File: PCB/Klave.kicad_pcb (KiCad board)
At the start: 2 copper layers, 156.3 x 127.5 mm, 87 parts, among them J1 6P6C, J2 OLED, SW0 Reset, SW1 0:0, SW10 1:3, SW11 1:4, SW12 1:5, SW13 2:0, SW14 2:1, SW15 2:2, SW16 2:3, SW17 2:4, SW18 2:5, SW19 3:0, SW2 0:1, SW20 3:1, SW21 3:2, SW22 3:3, SW23 3:4, SW24 3:5, SW26 4:1, SW27 4:2, SW28 4:3, SW29 4:4, SW3 0:2, SW30 4:5, SW35 5:4, SW36 5:5, SW4 0:3, SW5 0:4, SW6 0:5, SW7 1:0, SW8 1:1, SW9 1:2, U1 ProMicro

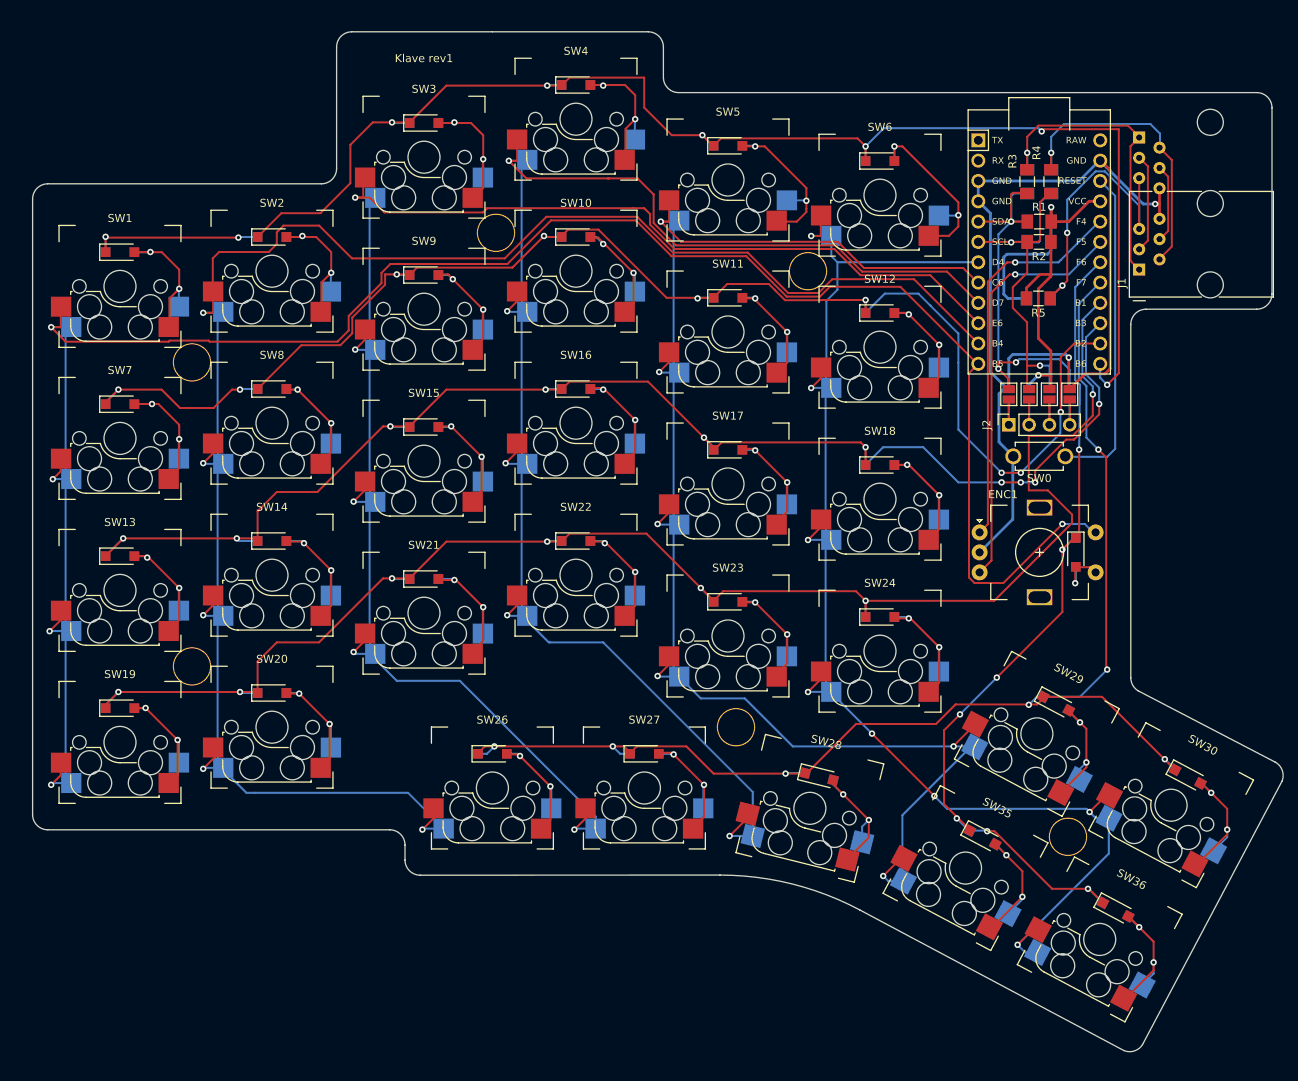
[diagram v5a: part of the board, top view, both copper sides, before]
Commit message: Add GND vias
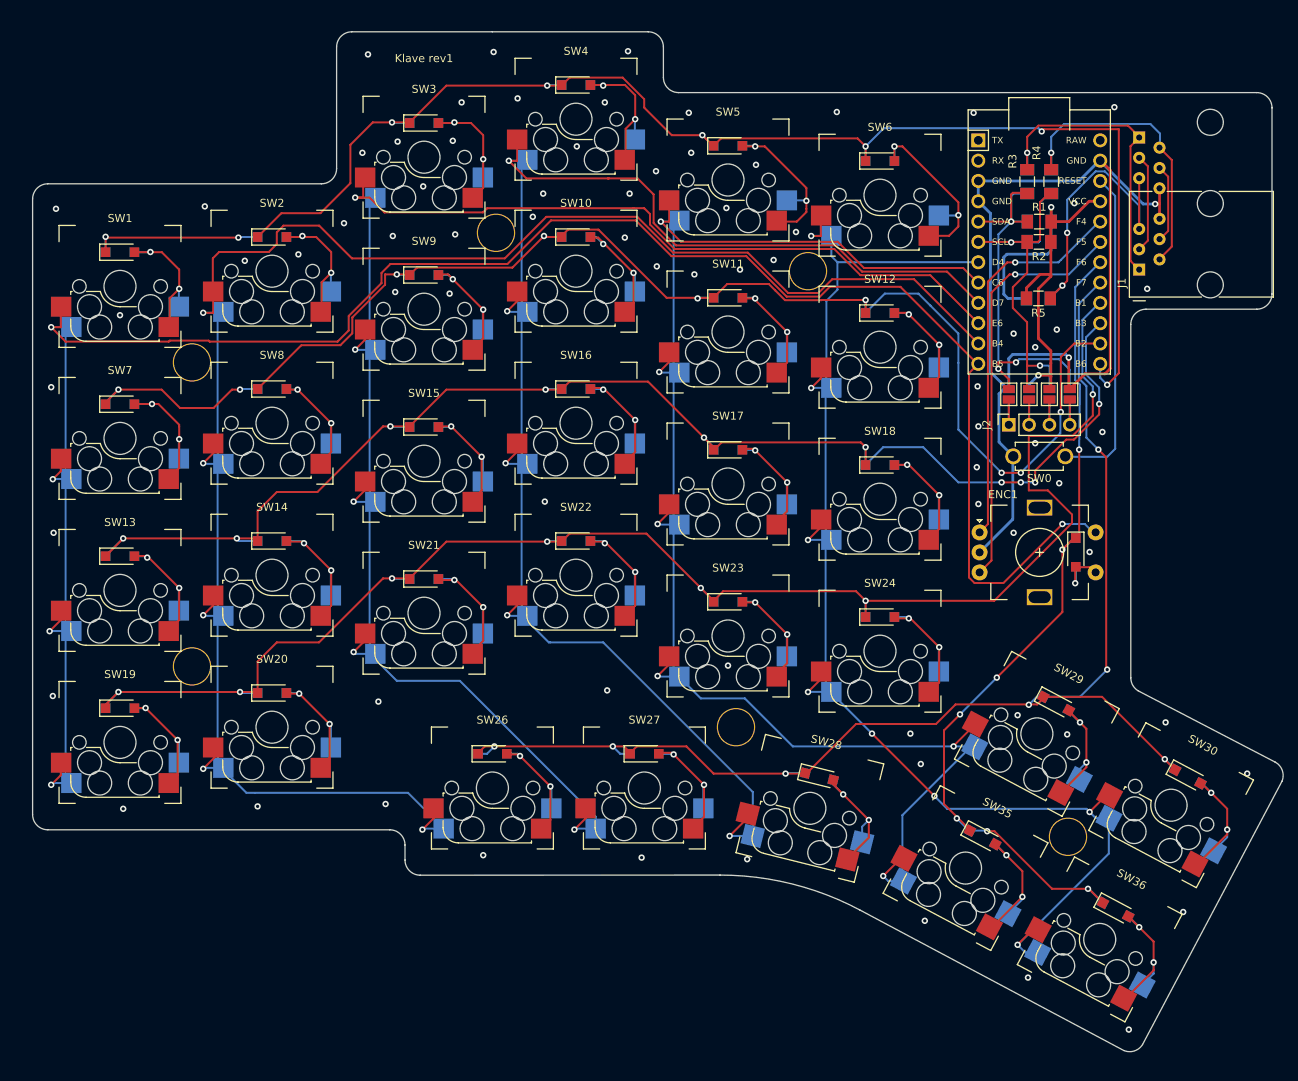
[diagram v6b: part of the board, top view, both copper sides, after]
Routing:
- net row0: track 194.5 -> 192.9 mm
- net GND: vias 2 -> 77
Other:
- rule trace_min: 0.2 -> 0.25
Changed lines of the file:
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@@
     (thickness 1.6)
     (drawings 36)
-    (tracks 1093)
+    (tracks 1169)
     (zones 0)
     (modules 87)
@@
     (zone_clearance 0.508)
     (zone_45_only no)
-    (trace_min 0.2)
+    (trace_min 0.25)
     (via_size 0.8)
     (via_drill 0.4)
@@
   (segment (start 158.626699 69.831301) (end 161.128625 69.831301) (width 0.35) (layer F.Cu) (net 34))
   (segment (start 161.779301 44.379301) (end 160.6 43.2) (width 0.35) (layer F.Cu) (net 34))
+  (via (at 160.8 77.1) (size 0.8) (drill 0.4) (layers F.Cu B.Cu) (net 34))
+  (via (at 157.3 48.5) (size 0.8) (drill 0.4) (layers F.Cu B.Cu) (net 34))
+  (via (at 114 106.3) (size 0.8) (drill 0.4) (layers F.Cu B.Cu) (net 34))
+  (via (at 136.8 114.8) (size 0.8) (drill 0.4) (layers F.Cu B.Cu) (net 34))
+  (via (at 138.1 118.6) (size 0.8) (drill 0.4) (layers F.Cu B.Cu) (net 34))
+  (via (at 149.7 89.7) (size 0.8) (drill 0.4) (layers F.Cu B.Cu) (net 34))
+  (via (at 155.4 83.5) (size 0.8) (drill 0.4) (layers F.Cu B.Cu) (net 34))
+  (via (at 145.3 86.1) (size 0.8) (drill 0.4) (layers F.Cu B.Cu) (net 34))
+  (via (at 145.1 81.5) (size 0.8) (drill 0.4) (layers F.Cu B.Cu) (net 34))
+  (via (at 145.3 76.4) (size 0.8) (drill 0.4) (layers F.Cu B.Cu) (net 34))
+  (via (at 145.2 71.4) (size 0.8) (drill 0.4) (layers F.Cu B.Cu) (net 34))
+  (via (at 149.7 64.8) (size 0.8) (drill 0.4) (layers F.Cu B.Cu) (net 34))
+  (via (at 152.4 66.5) (size 0.8) (drill 0.4) (layers F.Cu B.Cu) (net 34))
+  (via (at 155.1 64.3) (size 0.8) (drill 0.4) (layers F.Cu B.Cu) (net 34))
+  (via (at 119.7 55.6) (size 0.8) (drill 0.4) (layers F.Cu B.Cu) (net 34))
+  (via (at 115.5 56.8) (size 0.8) (drill 0.4) (layers F.Cu B.Cu) (net 34))
+  (via (at 109.8 57.4) (size 0.8) (drill 0.4) (layers F.Cu B.Cu) (net 34))
+  (via (at 105.1 56.4) (size 0.8) (drill 0.4) (layers F.Cu B.Cu) (net 34))
+  (via (at 101.1 52.8) (size 0.8) (drill 0.4) (layers F.Cu B.Cu) (net 34))
+  (via (at 90.9 47.3) (size 0.8) (drill 0.4) (layers F.Cu B.Cu) (net 34))
+  (via (at 101.7 47.3) (size 0.8) (drill 0.4) (layers F.Cu B.Cu) (net 34))
+  (via (at 105 44.5) (size 0.8) (drill 0.4) (layers F.Cu B.Cu) (net 34))
+  (via (at 109.4 42.2) (size 0.8) (drill 0.4) (layers F.Cu B.Cu) (net 34))
+  (via (at 117.5 43.7) (size 0.8) (drill 0.4) (layers F.Cu B.Cu) (net 34))
+  (via (at 98.6 35.9) (size 0.8) (drill 0.4) (layers F.Cu B.Cu) (net 34))
+  (via (at 80.7 35.9) (size 0.8) (drill 0.4) (layers F.Cu B.Cu) (net 34))
+  (via (at 87.7 35.4) (size 0.8) (drill 0.4) (layers F.Cu B.Cu) (net 34))
+  (via (at 79.9 52.4) (size 0.8) (drill 0.4) (layers F.Cu B.Cu) (net 34))
+  (via (at 72.1 52.6) (size 0.8) (drill 0.4) (layers F.Cu B.Cu) (net 34))
+  (via (at 66 51) (size 0.8) (drill 0.4) (layers F.Cu B.Cu) (net 34))
+  (via (at 60.3 54.9) (size 0.8) (drill 0.4) (layers F.Cu B.Cu) (net 34))
+  (via (at 79.6 40.7) (size 0.8) (drill 0.4) (layers F.Cu B.Cu) (net 34))
+  (via (at 72.7 40.8) (size 0.8) (drill 0.4) (layers F.Cu B.Cu) (net 34))
+  (via (at 68.3 42.2) (size 0.8) (drill 0.4) (layers F.Cu B.Cu) (net 34))
+  (via (at 38 62.5) (size 0.8) (drill 0.4) (layers F.Cu B.Cu) (net 34))
+  (via (at 53.6 55.7) (size 0.8) (drill 0.4) (layers F.Cu B.Cu) (net 34))
+  (via (at 30 49.2) (size 0.8) (drill 0.4) (layers F.Cu B.Cu) (net 34))
+  (via (at 48.6 48.9) (size 0.8) (drill 0.4) (layers F.Cu B.Cu) (net 34))
+  (via (at 69 29.9) (size 0.8) (drill 0.4) (layers F.Cu B.Cu) (net 34))
+  (via (at 84.7 29.6) (size 0.8) (drill 0.4) (layers F.Cu B.Cu) (net 34))
+  (via (at 101.5 29.5) (size 0.8) (drill 0.4) (layers F.Cu B.Cu) (net 34))
+  (via (at 109.1 37.2) (size 0.8) (drill 0.4) (layers F.Cu B.Cu) (net 34))
+  (via (at 127.6 37.1) (size 0.8) (drill 0.4) (layers F.Cu B.Cu) (net 34))
+  (via (at 144.7 37.2) (size 0.8) (drill 0.4) (layers F.Cu B.Cu) (net 34))
+  (via (at 162.3 36.5) (size 0.8) (drill 0.4) (layers F.Cu B.Cu) (net 34))
+  (via (at 166.4 59.2) (size 0.8) (drill 0.4) (layers F.Cu B.Cu) (net 34))
+  (via (at 178.9 119.8) (size 0.8) (drill 0.4) (layers F.Cu B.Cu) (net 34))
+  (via (at 168.7 113.4) (size 0.8) (drill 0.4) (layers F.Cu B.Cu) (net 34))
+  (via (at 170.9 137.1) (size 0.8) (drill 0.4) (layers F.Cu B.Cu) (net 34))
+  (via (at 164.1 151.8) (size 0.8) (drill 0.4) (layers F.Cu B.Cu) (net 34))
+  (via (at 151.5 145.3) (size 0.8) (drill 0.4) (layers F.Cu B.Cu) (net 34))
+  (via (at 138.6 138.2) (size 0.8) (drill 0.4) (layers F.Cu B.Cu) (net 34))
+  (via (at 116.4 130.5) (size 0.8) (drill 0.4) (layers F.Cu B.Cu) (net 34))
+  (via (at 103.2 130.3) (size 0.8) (drill 0.4) (layers F.Cu B.Cu) (net 34))
+  (via (at 83.4 130) (size 0.8) (drill 0.4) (layers F.Cu B.Cu) (net 34))
+  (via (at 71.2 123.6) (size 0.8) (drill 0.4) (layers F.Cu B.Cu) (net 34))
+  (via (at 55.2 123.9) (size 0.8) (drill 0.4) (layers F.Cu B.Cu) (net 34))
+  (via (at 38.4 124.2) (size 0.8) (drill 0.4) (layers F.Cu B.Cu) (net 34))
+  (via (at 29.6 110.1) (size 0.8) (drill 0.4) (layers F.Cu B.Cu) (net 34))
+  (via (at 29.7 89.7) (size 0.8) (drill 0.4) (layers F.Cu B.Cu) (net 34))
+  (via (at 29.4 71.5) (size 0.8) (drill 0.4) (layers F.Cu B.Cu) (net 34))
+  (via (at 70.3 110.8) (size 0.8) (drill 0.4) (layers F.Cu B.Cu) (net 34))
+  (via (at 98.9 109.4) (size 0.8) (drill 0.4) (layers F.Cu B.Cu) (net 34))
+  (via (at 91.1 85.8) (size 0.8) (drill 0.4) (layers F.Cu B.Cu) (net 34))
+  (via (at 72.4 59.6) (size 0.8) (drill 0.4) (layers F.Cu B.Cu) (net 34))
+  (via (at 79.2 59.8) (size 0.8) (drill 0.4) (layers F.Cu B.Cu) (net 34))
+  (via (at 75.9 46.4) (size 0.8) (drill 0.4) (layers F.Cu B.Cu) (net 34))
+  (via (at 95.1 41.4) (size 0.8) (drill 0.4) (layers F.Cu B.Cu) (net 34))
+  (via (at 113.8 49.1) (size 0.8) (drill 0.4) (layers F.Cu B.Cu) (net 34))
+  (via (at 122.5 52.1) (size 0.8) (drill 0.4) (layers F.Cu B.Cu) (net 34))
+  (via (at 156.4 114.9) (size 0.8) (drill 0.4) (layers F.Cu B.Cu) (net 34))
+  (via (at 150.2 112.5) (size 0.8) (drill 0.4) (layers F.Cu B.Cu) (net 34))
+  (via (at 159.2 92.1) (size 0.8) (drill 0.4) (layers F.Cu B.Cu) (net 34))
+  (via (at 89.6 50.2) (size 0.8) (drill 0.4) (layers F.Cu B.Cu) (net 34))
+  (via (at 152.4 78.5) (size 0.8) (drill 0.4) (layers F.Cu B.Cu) (net 34))
   (via (at 149.9 57.4) (size 0.8) (drill 0.4) (layers F.Cu B.Cu) (net 35))
   (segment (start 146.939311 59.660689) (end 149.2 57.4) (width 0.25) (layer F.Cu) (net 35))
@@
   (segment (start 36.2 54.625) (end 36.2 54.6) (width 0.25) (layer B.Cu) (net 42))
   (segment (start 110.8 40) (end 106.975 40) (width 0.25) (layer F.Cu) (net 42))
-  (segment (start 103.525001 36.550001) (end 103.525001 32.799999) (width 0.25) (layer F.Cu) (net 42))
   (segment (start 106.975 40) (end 103.525001 36.550001) (width 0.25) (layer F.Cu) (net 42))
-  (segment (start 103.525001 32.799999) (end 94.200001 32.799999) (width 0.25) (layer F.Cu) (net 42))
   (segment (start 110.8 40) (end 112.1 41.3) (width 0.25) (layer F.Cu) (net 42))
   (segment (start 58.17501 49.74999) (end 63.05001 49.74999) (width 0.25) (layer F.Cu) (net 42))
@@
   (segment (start 36.3 52.8) (end 36.2 52.7) (width 0.25) (layer F.Cu) (net 42))
   (segment (start 52.8 52.8) (end 36.3 52.8) (width 0.25) (layer F.Cu) (net 42))
+  (segment (start 100.836409 32.799999) (end 94.200001 32.799999) (width 0.25) (layer F.Cu) (net 42))
+  (segment (start 103.525001 35.488591) (end 100.836409 32.799999) (width 0.25) (layer F.Cu) (net 42))
+  (segment (start 103.525001 36.550001) (end 103.525001 35.488591) (width 0.25) (layer F.Cu) (net 42))
   (segment (start 37.875 71.725) (end 36.2 73.4) (width 0.25) (layer F.Cu) (net 43))
   (segment (start 131.2 62.225) (end 131.2 60.6) (width 0.25) (layer F.Cu) (net 43))

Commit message: Fix DRC errors
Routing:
- net row0: track 192.9 -> 195.3 mm
- net row5: track 108.1 -> 110.2 mm
- net row1: track 184.0 -> 186.0 mm
- net GND: vias 77 -> 82
